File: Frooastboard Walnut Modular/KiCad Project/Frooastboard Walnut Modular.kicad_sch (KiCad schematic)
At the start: 0 parts

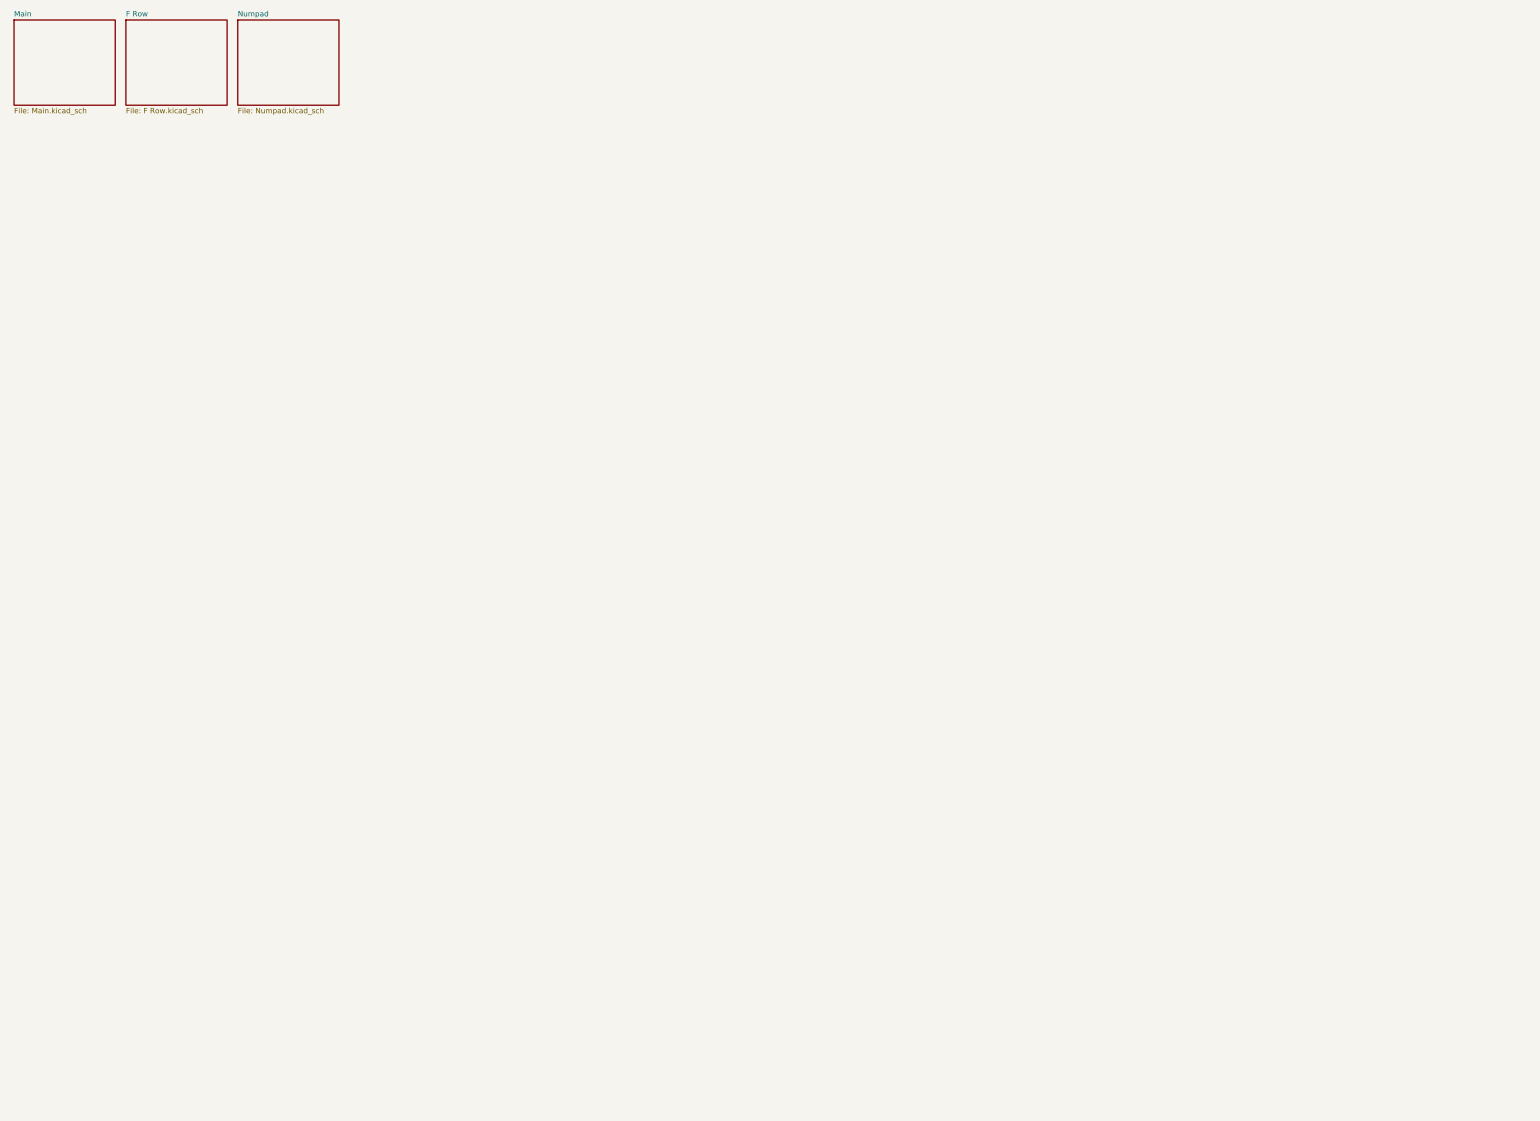
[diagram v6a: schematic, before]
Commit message: fix symbols and remove lck
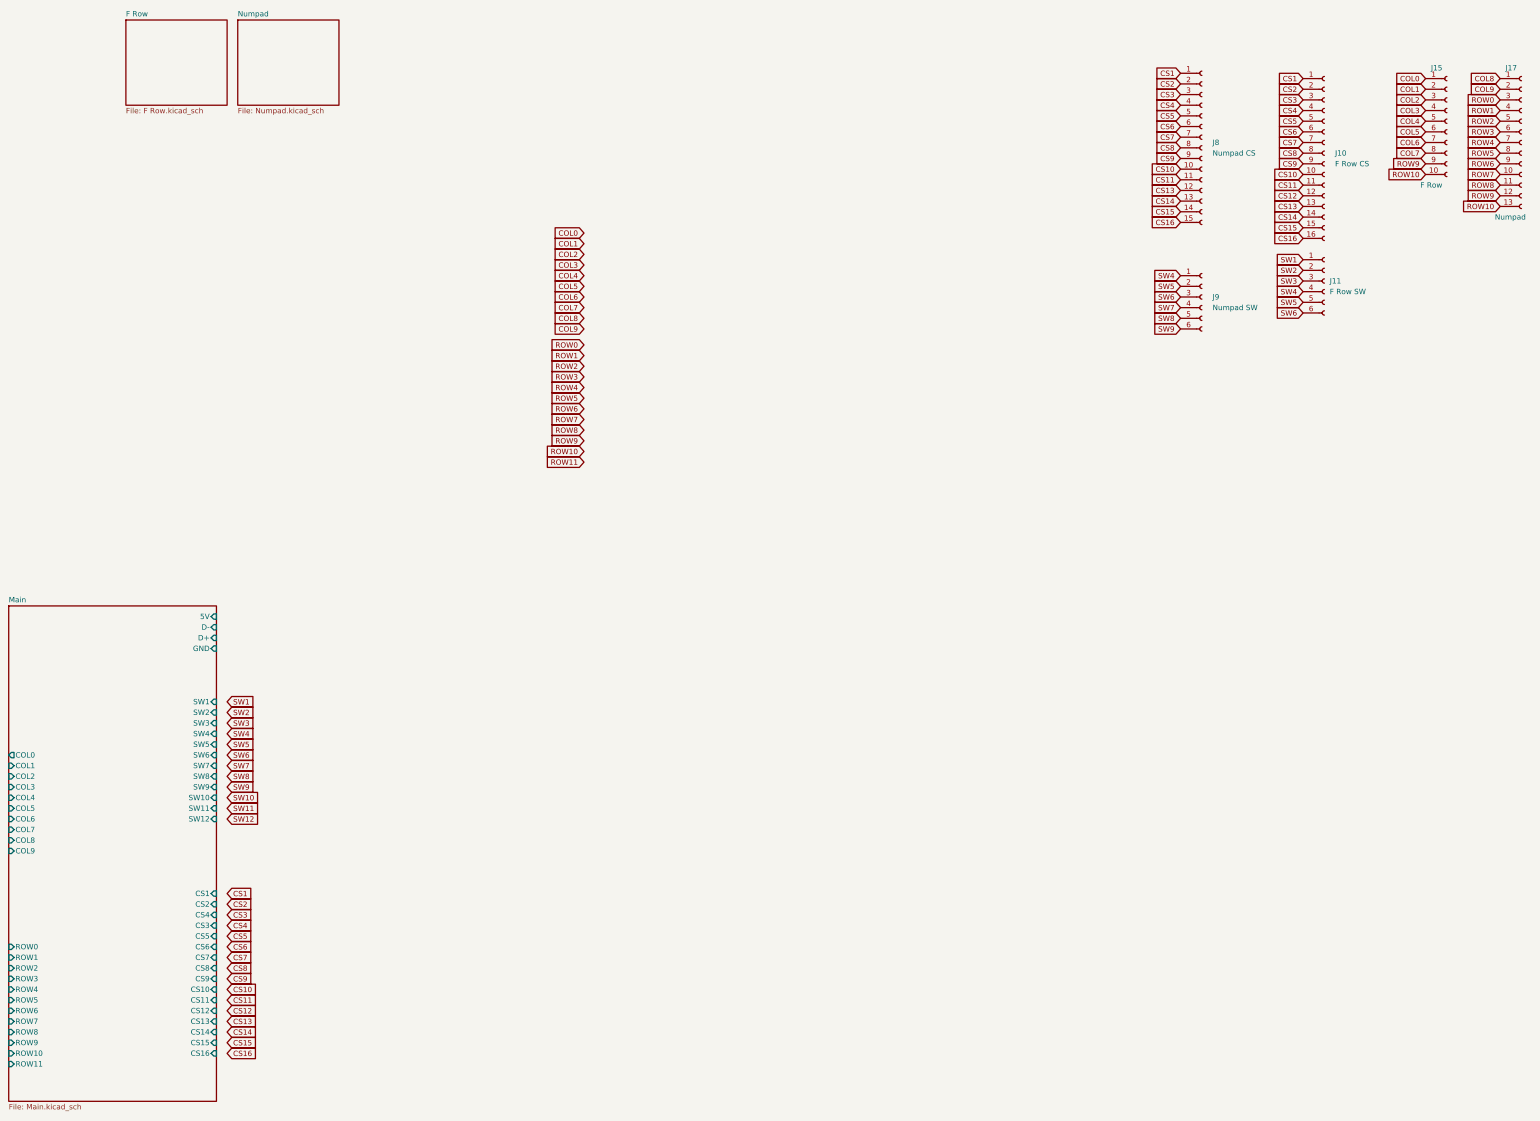
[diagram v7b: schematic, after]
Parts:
- added J10: F Row CS, Connector_PinHeader_1.27mm:PinHeader_1x16_P1.27mm_Vertical, symbol Connector:Conn_01x16_Socket
- added J11: F Row SW, Connector_PinHeader_1.27mm:PinHeader_1x06_P1.27mm_Vertical, symbol Connector:Conn_01x06_Socket
- added J15: F Row, Connector_PinHeader_1.27mm:PinHeader_1x10_P1.27mm_Vertical, symbol Connector:Conn_01x10_Socket
- added J17: Numpad, Connector_PinHeader_1.27mm:PinHeader_1x13_P1.27mm_Vertical, symbol Connector:Conn_01x13_Socket
- added J8: Numpad CS, Connector_PinHeader_1.27mm:PinHeader_1x16_P1.27mm_Vertical, symbol Connector:Conn_01x15_Socket
- added J9: Numpad SW, Connector_PinHeader_1.27mm:PinHeader_1x06_P1.27mm_Vertical, symbol Connector:Conn_01x06_Socket
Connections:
- new net COL0: J15.1 (Pin_1)
- new net COL1: J15.2 (Pin_2)
- new net COL2: J15.3 (Pin_3)
- new net COL3: J15.4 (Pin_4)
- new net COL4: J15.5 (Pin_5)
- new net COL5: J15.6 (Pin_6)
- new net COL6: J15.7 (Pin_7)
- new net COL7: J15.8 (Pin_8)
- new net COL8: J17.1 (Pin_1)
- new net COL9: J17.2 (Pin_2)
- new net CS1: J10.1 (Pin_1), J8.1 (Pin_1)
- new net CS10: J10.10 (Pin_10), J8.10 (Pin_10)
- new net CS11: J10.11 (Pin_11), J8.11 (Pin_11)
- new net CS12: J10.12 (Pin_12)
- new net CS13: J10.13 (Pin_13), J8.12 (Pin_12)
- new net CS14: J10.14 (Pin_14), J8.13 (Pin_13)
- new net CS15: J10.15 (Pin_15), J8.14 (Pin_14)
- new net CS16: J10.16 (Pin_16), J8.15 (Pin_15)
- new net CS2: J10.2 (Pin_2), J8.2 (Pin_2)
- new net CS3: J10.3 (Pin_3), J8.3 (Pin_3)
- new net CS4: J10.4 (Pin_4), J8.4 (Pin_4)
- new net CS5: J10.5 (Pin_5), J8.5 (Pin_5)
- new net CS6: J10.6 (Pin_6), J8.6 (Pin_6)
- new net CS7: J10.7 (Pin_7), J8.7 (Pin_7)
- new net CS8: J10.8 (Pin_8), J8.8 (Pin_8)
- new net CS9: J10.9 (Pin_9), J8.9 (Pin_9)
- new net ROW0: J17.3 (Pin_3)
- new net ROW1: J17.4 (Pin_4)
- new net ROW10: J15.10 (Pin_10), J17.13 (Pin_13)
- new net ROW2: J17.5 (Pin_5)
- new net ROW3: J17.6 (Pin_6)
- new net ROW4: J17.7 (Pin_7)
- new net ROW5: J17.8 (Pin_8)
- new net ROW6: J17.9 (Pin_9)
- new net ROW7: J17.10 (Pin_10)
- new net ROW8: J17.11 (Pin_11)
- new net ROW9: J15.9 (Pin_9), J17.12 (Pin_12)
- new net SW1: J11.1 (Pin_1)
- new net SW2: J11.2 (Pin_2)
- new net SW3: J11.3 (Pin_3)
- new net SW4: J11.4 (Pin_4), J9.1 (Pin_1)
- new net SW5: J11.5 (Pin_5), J9.2 (Pin_2)
- new net SW6: J11.6 (Pin_6), J9.3 (Pin_3)
- new net SW7: J9.4 (Pin_4)
- new net SW8: J9.5 (Pin_5)
- new net SW9: J9.6 (Pin_6)
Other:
- sheet Main ports: added 5V, COL0, COL1, COL2, COL3, COL4, COL5, COL6, COL7, COL8, COL9, CS1, CS10, CS11, CS12, CS13, CS14, CS15, CS16, CS2, CS3, CS4, CS5, CS6, CS7, CS8, CS9, D+, D-, GND, ROW0, ROW1, ROW10, ROW11, ROW2, ROW3, ROW4, ROW5, ROW6, ROW7, ROW8, ROW9, SW1, SW10, SW11, SW12, SW2, SW3, SW4, SW5, SW6, SW7, SW8, SW9; removed none

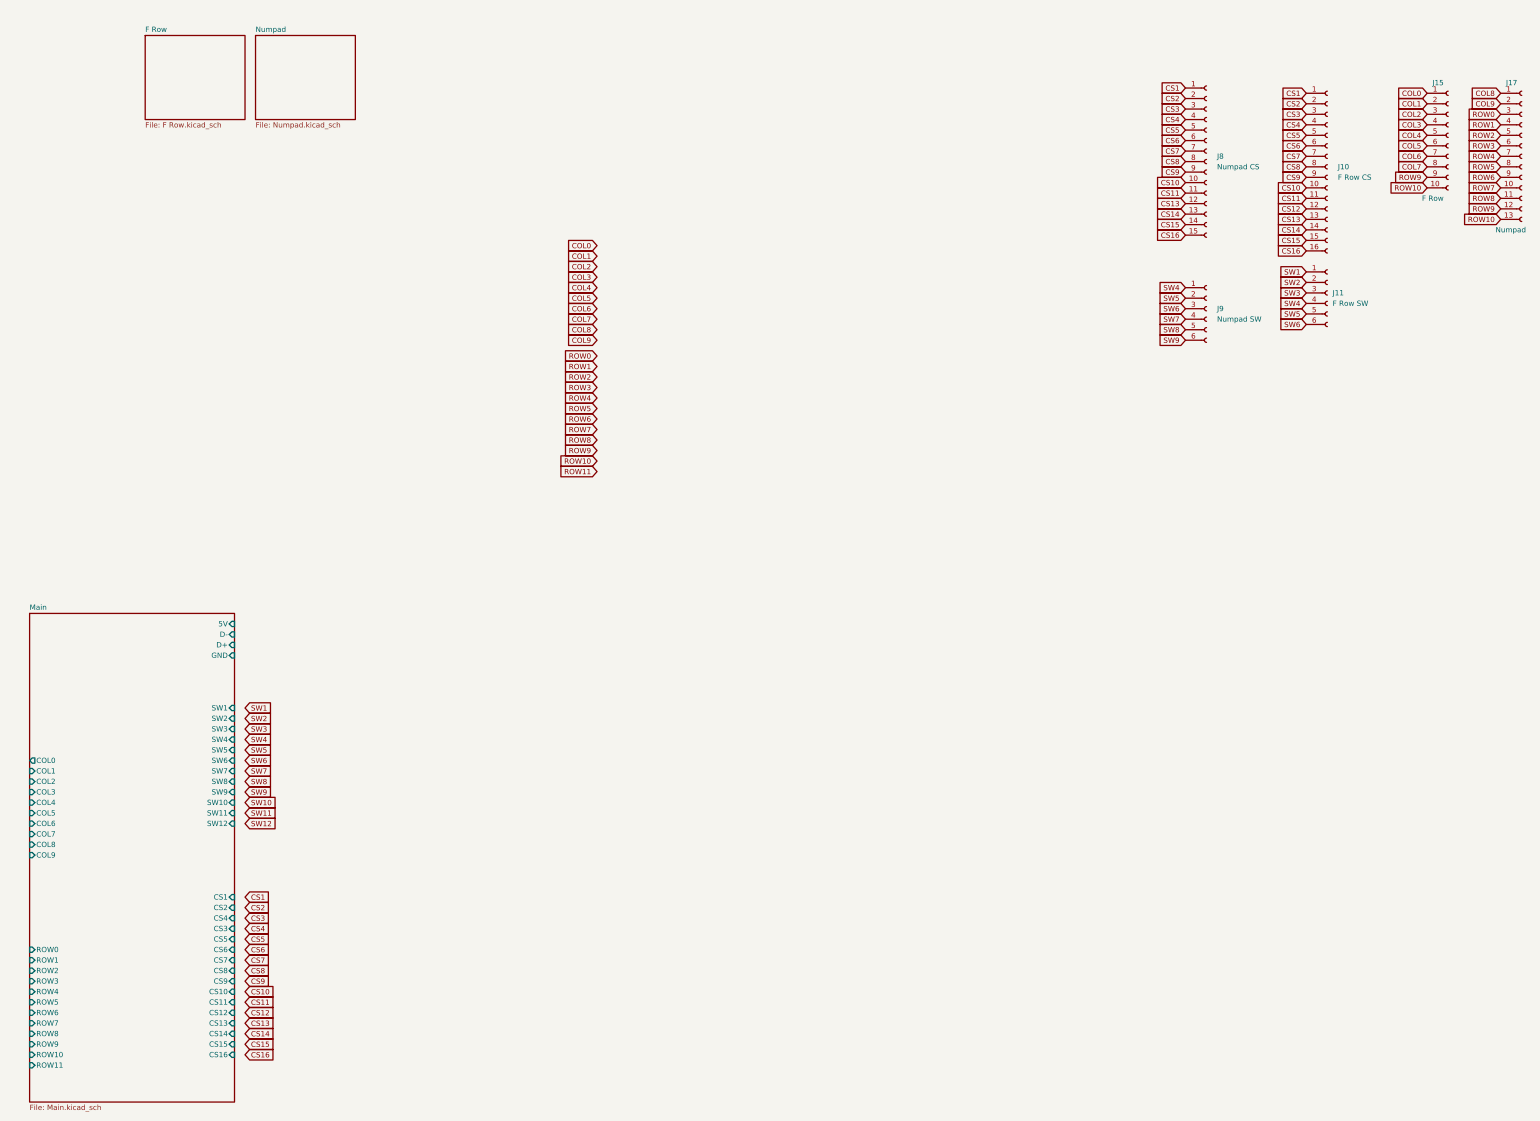
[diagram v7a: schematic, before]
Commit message: almost finished bus stuff connector fpc
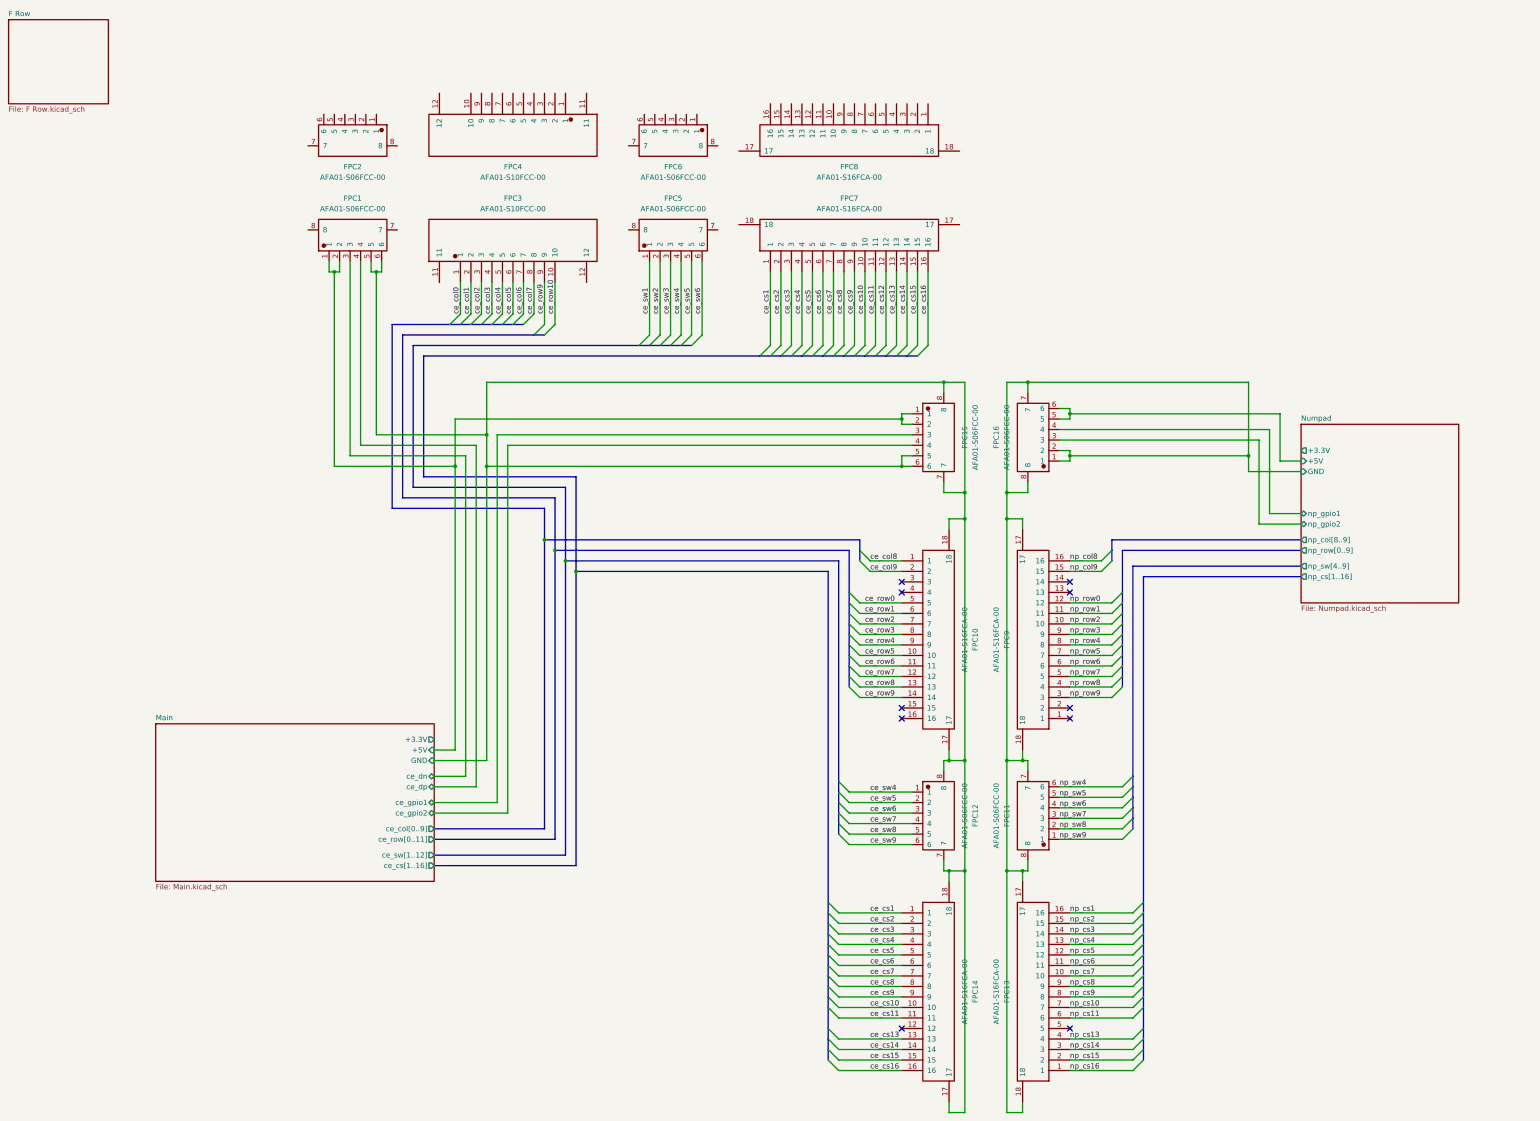
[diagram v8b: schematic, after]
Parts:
- removed J10: F Row CS, Connector_PinHeader_1.27mm:PinHeader_1x16_P1.27mm_Vertical, symbol Connector:Conn_01x16_Socket
- removed J11: F Row SW, Connector_PinHeader_1.27mm:PinHeader_1x06_P1.27mm_Vertical, symbol Connector:Conn_01x06_Socket
- removed J15: F Row, Connector_PinHeader_1.27mm:PinHeader_1x10_P1.27mm_Vertical, symbol Connector:Conn_01x10_Socket
- removed J17: Numpad, Connector_PinHeader_1.27mm:PinHeader_1x13_P1.27mm_Vertical, symbol Connector:Conn_01x13_Socket
- removed J8: Numpad CS, Connector_PinHeader_1.27mm:PinHeader_1x16_P1.27mm_Vertical, symbol Connector:Conn_01x15_Socket
- removed J9: Numpad SW, Connector_PinHeader_1.27mm:PinHeader_1x06_P1.27mm_Vertical, symbol Connector:Conn_01x06_Socket
- added FPC1, FPC11, FPC12, FPC15, FPC16, FPC2, FPC5, FPC6: AFA01-S06FCC-00, kicad_lceda:FPC-SMD_6P-P1.00_AFA01-S06, symbol AFA01-SXXFCX-00:AFA01-S06FCC-00
- added FPC10, FPC13, FPC14, FPC7, FPC8, FPC9: AFA01-S16FCA-00, kicad_lceda:FPC-SMD_P1.00-16P_FGS-XJ-H2.0, symbol AFA01-SXXFCX-00:AFA01-S16FCA-00
- added FPC3, FPC4: AFA01-S10FCC-00, kicad_lceda:FPC-SMD_AFA01-S10FCC-00, symbol AFA01-SXXFCX-00:AFA01-S10FCC-00
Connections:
- net Main/GND: now also FPC1.5, FPC1.6, FPC10.17, FPC10.18, FPC12.7, FPC12.8, FPC14.17, FPC14.18, FPC15.5, FPC15.6, FPC15.7, FPC15.8
- new net Main/+5V: FPC1.1, FPC1.2, FPC15.1, FPC15.2
- new net Main/ce_dn: FPC1.3
- new net Main/ce_dp: FPC1.4
- new net Main/ce_gpio1: FPC15.3
- new net Main/ce_gpio2: FPC15.4
- new net Numpad/+5V: FPC16.5, FPC16.6
- new net Numpad/GND: FPC11.7, FPC11.8, FPC13.17, FPC13.18, FPC16.1, FPC16.2, FPC16.7, FPC16.8, FPC9.17, FPC9.18
- new net Numpad/np_gpio1: FPC16.4
- new net Numpad/np_gpio2: FPC16.3
- new net ce_col0: FPC3.1
- new net ce_col1: FPC3.2
- new net ce_col2: FPC3.3
- new net ce_col3: FPC3.4
- new net ce_col4: FPC3.5
- new net ce_col5: FPC3.6
- new net ce_col6: FPC3.7
- new net ce_col7: FPC3.8
- new net ce_col8: FPC10.1
- new net ce_col9: FPC10.2
- new net ce_cs1: FPC14.1, FPC7.1
- new net ce_cs10: FPC14.10, FPC7.10
- new net ce_cs11: FPC14.11, FPC7.11
- new net ce_cs12: FPC7.12
- new net ce_cs13: FPC14.13, FPC7.13
- new net ce_cs14: FPC14.14, FPC7.14
- new net ce_cs15: FPC14.15, FPC7.15
- new net ce_cs16: FPC14.16, FPC7.16
- new net ce_cs2: FPC14.2, FPC7.2
- new net ce_cs3: FPC14.3, FPC7.3
- new net ce_cs4: FPC14.4, FPC7.4
- new net ce_cs5: FPC14.5, FPC7.5
- new net ce_cs6: FPC14.6, FPC7.6
- new net ce_cs7: FPC14.7, FPC7.7
- new net ce_cs8: FPC14.8, FPC7.8
- new net ce_cs9: FPC14.9, FPC7.9
- new net ce_row0: FPC10.5
- new net ce_row1: FPC10.6
- new net ce_row10: FPC3.10
- new net ce_row2: FPC10.7
- new net ce_row3: FPC10.8
- new net ce_row4: FPC10.9
- new net ce_row5: FPC10.10
- new net ce_row6: FPC10.11
- new net ce_row7: FPC10.12
- new net ce_row8: FPC10.13
- new net ce_row9: FPC10.14, FPC3.9
- new net ce_sw1: FPC5.1
- new net ce_sw2: FPC5.2
- new net ce_sw3: FPC5.3
- new net ce_sw4: FPC12.1, FPC5.4
- new net ce_sw5: FPC12.2, FPC5.5
- new net ce_sw6: FPC12.3, FPC5.6
- new net ce_sw7: FPC12.4
- new net ce_sw8: FPC12.5
- new net ce_sw9: FPC12.6
- new net np_col8: FPC9.16
- new net np_col9: FPC9.15
- new net np_cs1: FPC13.16
- new net np_cs10: FPC13.7
- new net np_cs11: FPC13.6
- new net np_cs13: FPC13.4
- new net np_cs14: FPC13.3
- new net np_cs15: FPC13.2
- new net np_cs16: FPC13.1
- new net np_cs2: FPC13.15
- new net np_cs3: FPC13.14
- new net np_cs4: FPC13.13
- new net np_cs5: FPC13.12
- new net np_cs6: FPC13.11
- new net np_cs7: FPC13.10
- new net np_cs8: FPC13.9
- new net np_cs9: FPC13.8
- new net np_row0: FPC9.12
- new net np_row1: FPC9.11
- new net np_row2: FPC9.10
- new net np_row3: FPC9.9
- new net np_row4: FPC9.8
- new net np_row5: FPC9.7
- new net np_row6: FPC9.6
- new net np_row7: FPC9.5
- new net np_row8: FPC9.4
- new net np_row9: FPC9.3
- new net np_sw4: FPC11.6
- new net np_sw5: FPC11.5
- new net np_sw6: FPC11.4
- new net np_sw7: FPC11.3
- new net np_sw8: FPC11.2
- new net np_sw9: FPC11.1
- no-connect marks 0 -> 10
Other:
- sheet Main ports: added +3.3V, +5V, ce_col[0..9], ce_cs[1..16], ce_dn, ce_dp, ce_gpio1, ce_gpio2, ce_row[0..11], ce_sw[1..12]; removed 5V, COL0, COL1, COL2, COL3, COL4, COL5, COL6, COL7, COL8, COL9, CS1, CS10, CS11, CS12, CS13, CS14, CS15, CS16, CS2, CS3, CS4, CS5, CS6, CS7, CS8, CS9, D+, D-, ROW0, ROW1, ROW10, ROW11, ROW2, ROW3, ROW4, ROW5, ROW6, ROW7, ROW8, ROW9, SW1, SW10, SW11, SW12, SW2, SW3, SW4, SW5, SW6, SW7, SW8, SW9
- sheet Numpad ports: added +3.3V, +5V, GND, np_col[8..9], np_cs[1..16], np_gpio1, np_gpio2, np_row[0..9], np_sw[4..9]; removed none
